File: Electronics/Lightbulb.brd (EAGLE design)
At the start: 65 x 47 mm, 22 parts, among them IC2 7805L

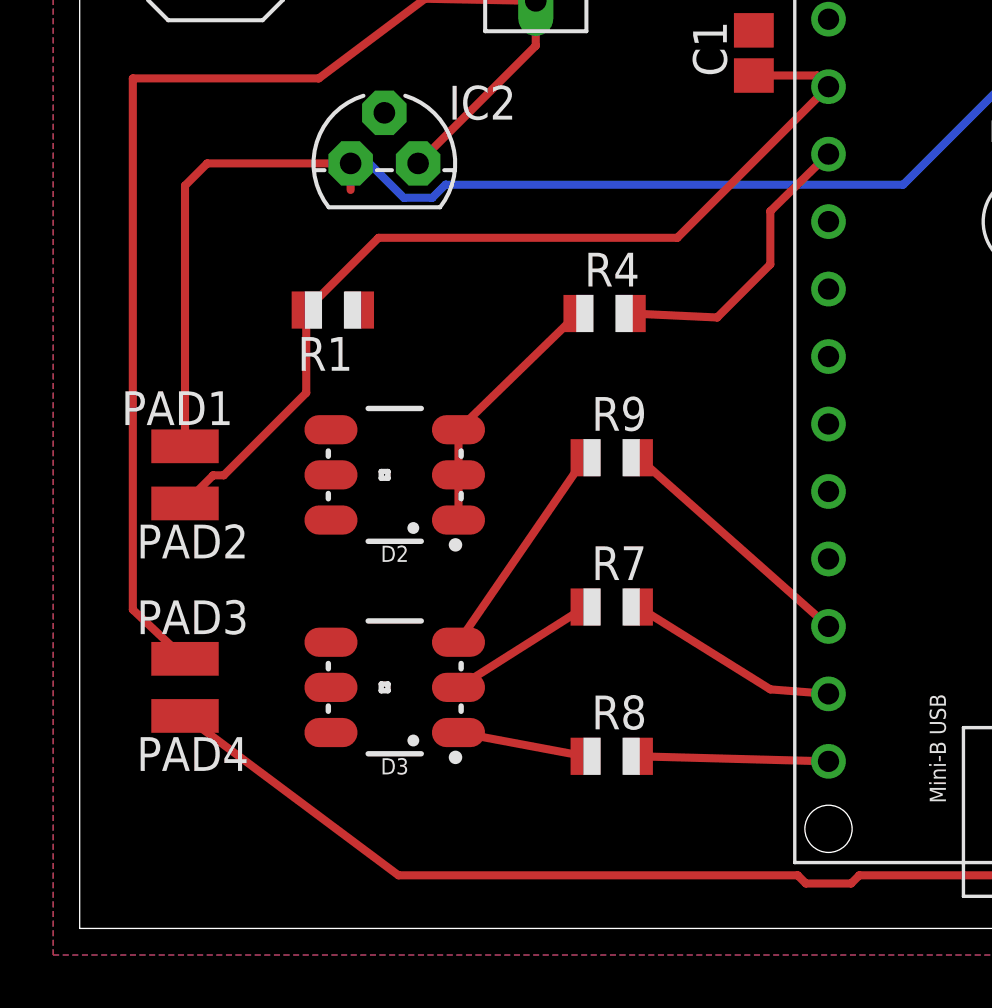
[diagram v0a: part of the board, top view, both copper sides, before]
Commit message: Moving switches and LEDs to bottom side of board
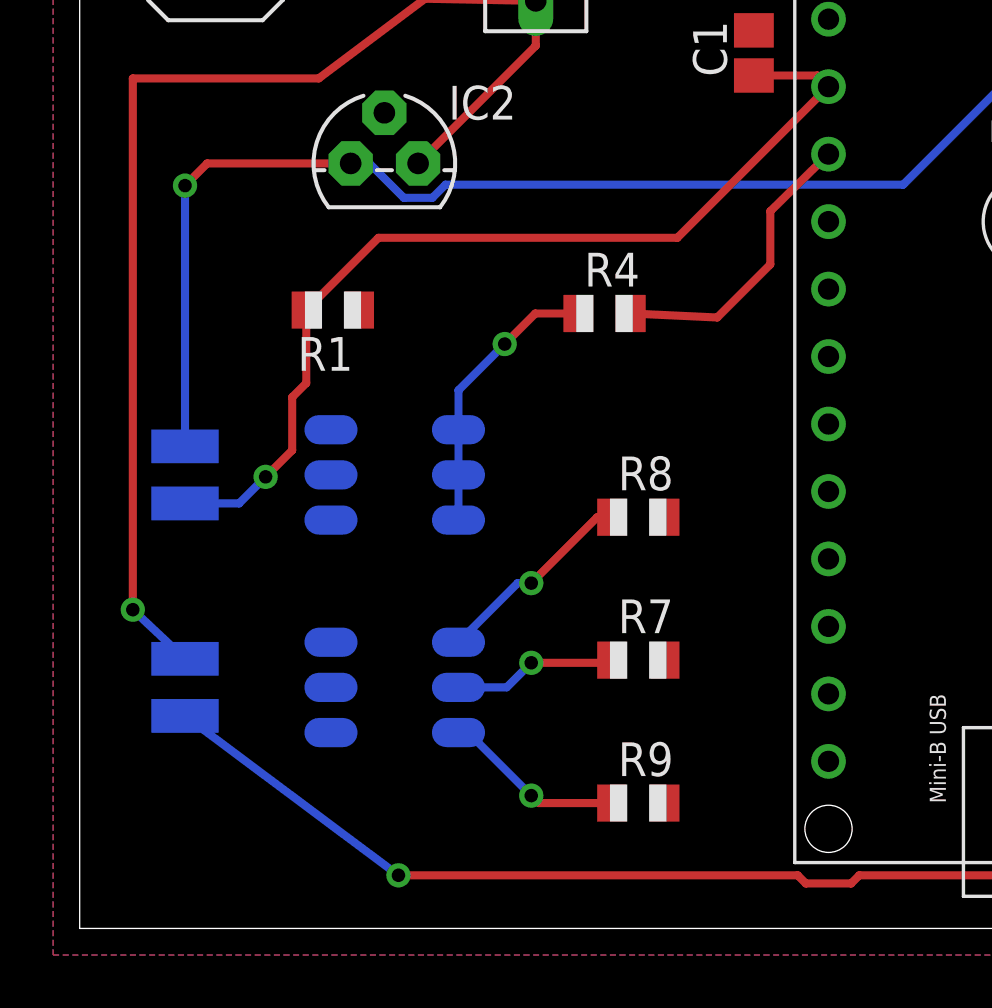
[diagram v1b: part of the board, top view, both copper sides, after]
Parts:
- moved R9 13.0 mm to (21.0, 4.72)
- moved R8 9.06 mm to (21.0, 15.5)
- moved R7 2.24 mm to (21.0, 10.1)
- flipped D2 to the bottom, turned to 0 degrees
- flipped D3 to the bottom, turned to 0 degrees
- flipped PAD1 to the bottom
- flipped PAD2 to the bottom
- flipped PAD3 to the bottom
- flipped PAD4 to the bottom
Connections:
- net N$12: now also ARDUINO_NANO1.28; no longer ARDUINO_NANO1.30
- net N$2: now also ARDUINO_NANO1.30; no longer ARDUINO_NANO1.28
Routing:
- net N$2: track 9.57 -> 0.00 mm
- net N$8: track 8.05 -> 0.00 mm
- net N$12: track 7.16 -> 0.00 mm
- net N$10: track 4.85 -> 7.72 mm, vias 0 -> 1
- net N$11: track 8.43 -> 6.87 mm, vias 0 -> 1
- net N$4: track 68.0 -> 67.0 mm, vias 0 -> 1
- net N$3: track 35.5 -> 36.5 mm, vias 0 -> 1
- net N$18: track 9.68 -> 10.6 mm, vias 0 -> 1
- net N$9: track 5.65 -> 6.19 mm, vias 0 -> 1
- net VCC: vias 0 -> 1
- net N$6: vias 2 -> 3

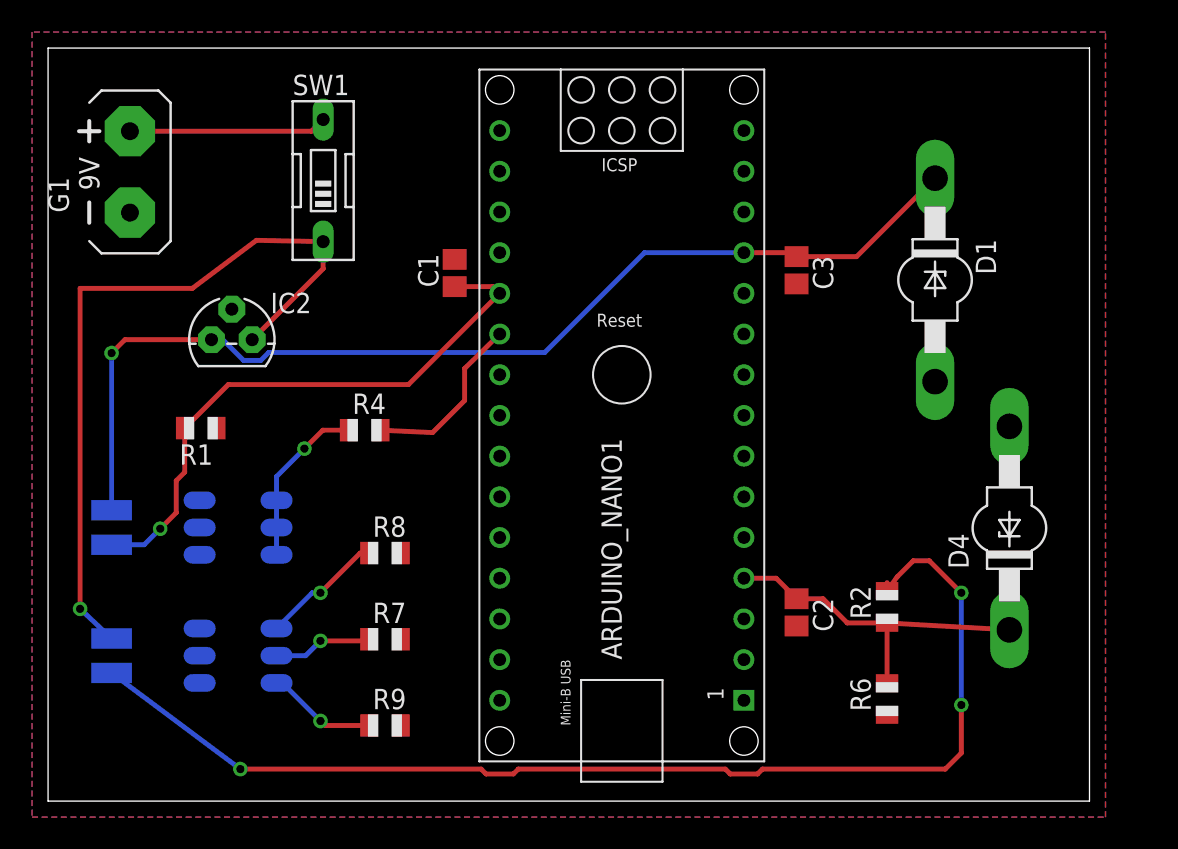
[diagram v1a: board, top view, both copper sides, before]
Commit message: Updated board layout to put master switch on back and added connections for RGB LED
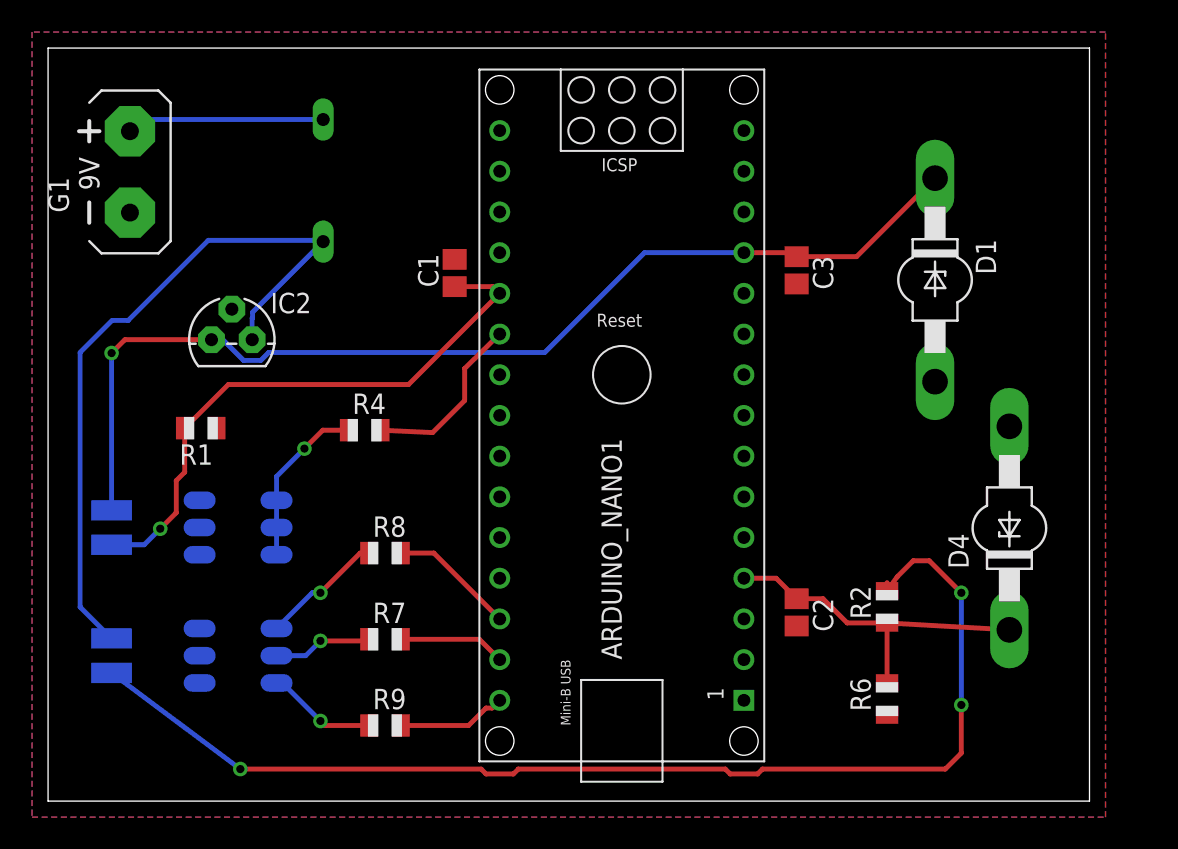
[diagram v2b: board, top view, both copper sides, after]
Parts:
- flipped SW1 to the bottom
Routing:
- net N$12: track 0.00 -> 7.86 mm
- net N$2: track 0.00 -> 6.81 mm
- net N$8: track 0.00 -> 6.69 mm
- net VCC: track 46.8 -> 44.7 mm, vias 1 -> 0
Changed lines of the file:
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@@
 <attribute name="VALUE" x="20.268" y="2.434" size="1.27" layer="27"/>
 </element>
-<element name="SW1" library="special" library_urn="urn:adsk.eagle:library:367" package="EDG-01" package3d_urn="urn:adsk.eagle:package:26661/1" value="" x="17.17" y="38.73">
-<attribute name="NAME" x="15.265" y="44.064" size="1.27" layer="25" ratio="10"/>
-<attribute name="VALUE" x="15.265" y="32.126" size="1.27" layer="27" ratio="10"/>
+<element name="SW1" library="special" library_urn="urn:adsk.eagle:library:367" package="EDG-01" package3d_urn="urn:adsk.eagle:package:26661/1" value="" x="17.17" y="38.73" rot="MR0">
+<attribute name="NAME" x="19.075" y="44.064" size="1.27" layer="26" ratio="10" rot="MR0"/>
+<attribute name="VALUE" x="19.075" y="32.126" size="1.27" layer="28" ratio="10" rot="MR0"/>
 </element>
 </elements>
@@
 <contactref element="IC2" pad="3"/>
 <contactref element="SW1" pad="1"/>
-<wire x1="17.17" y1="33.23" x2="12.74" y2="28.8" width="0.3048" layer="1"/>
-<wire x1="17.17" y1="34.92" x2="13" y2="35" width="0.3048" layer="1"/>
-<wire x1="13" y1="35" x2="9" y2="32" width="0.3048" layer="1"/>
-<wire x1="9" y1="32" x2="2" y2="32" width="0.3048" layer="1"/>
-<wire x1="2" y1="32" x2="2" y2="12" width="0.3048" layer="1"/>
-<wire x1="2" y1="12" x2="3.965" y2="10.15" width="0.3048" layer="16"/>
-<wire x1="17.17" y1="34.92" x2="17.17" y2="33.23" width="0.3048" layer="1"/>
-<via x="2" y="12" extent="1-16" drill="0.508"/>
+<wire x1="17.17" y1="34.92" x2="12.7654" y2="30.5154" width="0.3048" layer="16"/>
+<wire x1="12.7654" y1="30.5154" x2="12.7654" y2="30.168425" width="0.3048" layer="16"/>
+<wire x1="12.7654" y1="30.168425" x2="12.74" y2="30.143025" width="0.3048" layer="16"/>
+<wire x1="12.74" y1="30.143025" x2="12.74" y2="28.8" width="0.3048" layer="16"/>
+<wire x1="17.17" y1="34.92" x2="17.09" y2="35" width="0.3048" layer="16"/>
+<wire x1="5" y1="30" x2="4" y2="30" width="0.3048" layer="16"/>
+<wire x1="4" y1="30" x2="2" y2="28" width="0.3048" layer="16"/>
+<wire x1="2" y1="12.115" x2="3.965" y2="10.15" width="0.3048" layer="16"/>
+<wire x1="17.09" y1="35" x2="10" y2="35" width="0.3048" layer="16"/>
+<wire x1="10" y1="35" x2="5" y2="30" width="0.3048" layer="16"/>
+<wire x1="2" y1="28" x2="2" y2="12.115" width="0.3048" layer="16"/>
 </signal>
 <signal name="N$8">
 <contactref element="R7" pad="2"/>
 <contactref element="ARDUINO_NANO1" pad="29"/>
-<wire x1="22.03" y1="10.1" x2="28.19" y2="8.83" width="0" layer="19" extent="1-1"/>
+<wire x1="22.03" y1="10.1" x2="26.92" y2="10.1" width="0.3048" layer="1"/>
+<wire x1="26.92" y1="10.1" x2="28.19" y2="8.83" width="0.3048" layer="1"/>
 </signal>
 <signal name="N$1">
 <contactref element="G1" pad="+"/>
 <contactref element="SW1" pad="2"/>
-<wire x1="5.11" y1="41.81" x2="16.44" y2="41.81" width="0.3048" layer="1"/>
-<wire x1="16.44" y1="41.81" x2="17.17" y2="42.54" width="0.3048" layer="1"/>
+<wire x1="17.17" y1="42.54" x2="5.84" y2="42.54" width="0.3048" layer="16"/>
+<wire x1="5.84" y1="42.54" x2="5.11" y2="41.81" width="0.3048" layer="16"/>
 </signal>
 <signal name="N$2">
 <contactref element="ARDUINO_NANO1" pad="30"/>
 <contactref element="R9" pad="2"/>
-<wire x1="22.03" y1="4.72" x2="28.19" y2="6.29" width="0" layer="19" extent="1-1"/>
+<wire x1="22.03" y1="4.72" x2="26.25039375" y2="4.72" width="0.3048" layer="1"/>
+<wire x1="26.25039375" y1="4.72" x2="27.33779375" y2="5.8074" width="0.3048" layer="1"/>
+<wire x1="27.33779375" y1="5.8074" x2="27.7074" y2="5.8074" width="0.3048" layer="1"/>
+<wire x1="27.7074" y1="5.8074" x2="28.19" y2="6.29" width="0.3048" layer="1"/>
 </signal>
 <signal name="N$12">
 <contactref element="R8" pad="2"/>
 <contactref element="ARDUINO_NANO1" pad="28"/>
-<wire x1="22.03" y1="15.48" x2="28.19" y2="11.37" width="0" layer="19" extent="1-1"/>
+<wire x1="22.03" y1="15.48" x2="24.08" y2="15.48" width="0.3048" layer="1"/>
+<wire x1="24.08" y1="15.48" x2="28.19" y2="11.37" width="0.3048" layer="1"/>
 </signal>
 </signals>

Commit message: Correcting pad placement and connections on PCB
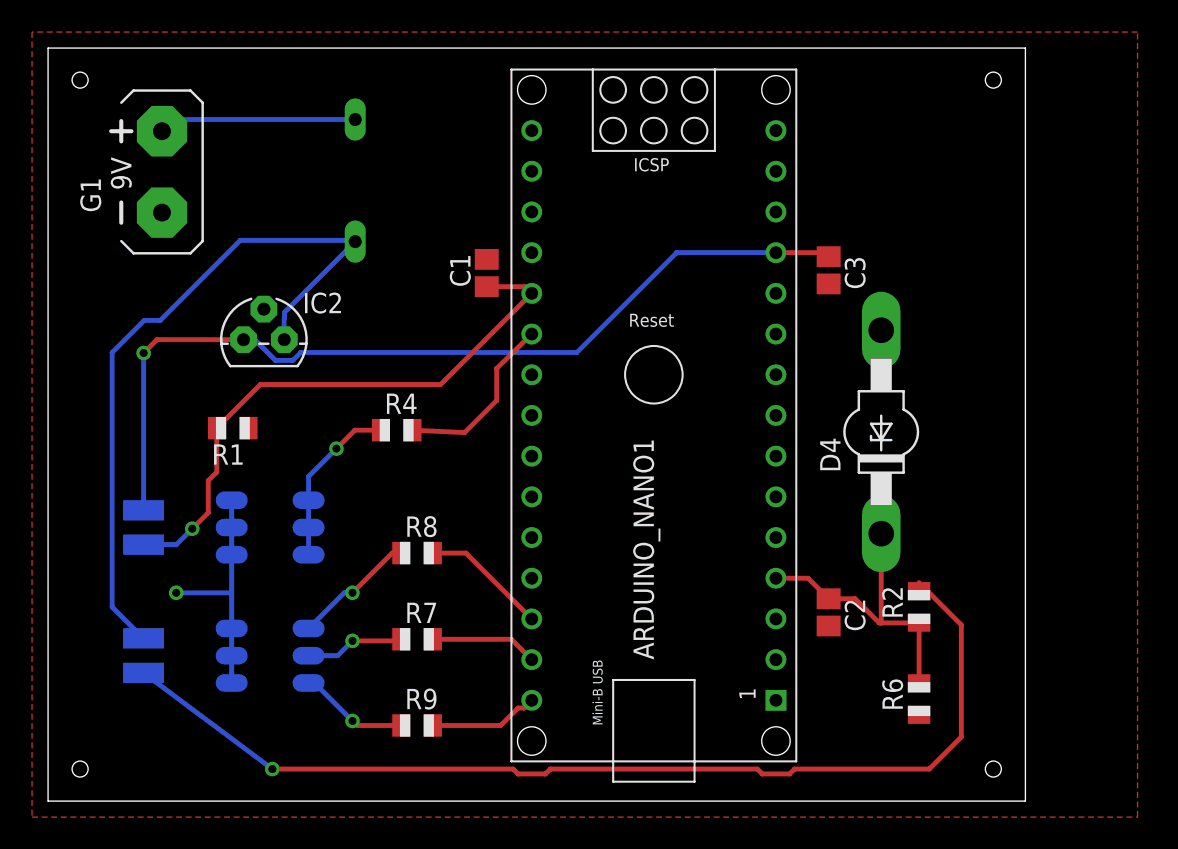
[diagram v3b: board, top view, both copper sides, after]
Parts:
- removed D1: 5.1V Zener, diode:SOD64Z12
- moved D4 10.0 mm to (52.0, 23.0)
- moved ARDUINO_NANO1 2.00 mm to (37.8, 26.6)
- moved C1 2.00 mm to (27.4, 33.0)
- moved C2 2.00 mm to (48.7, 11.8)
- moved C3 2.00 mm to (48.7, 33.1)
- moved D2 2.00 mm to (13.9, 17.1)
- moved D3 2.00 mm to (13.9, 9.07)
- moved G1 2.00 mm to (7.11, 39.3)
- moved IC2 2.00 mm to (13.5, 28.8)
- moved PAD1 2.00 mm to (5.96, 18.1)
- moved PAD2 2.00 mm to (5.96, 16.0)
- moved PAD3 2.00 mm to (5.96, 10.2)
- moved PAD4 2.00 mm to (5.96, 8.00)
- moved R1 2.00 mm to (11.5, 23.3)
- moved R2 2.00 mm to (54.4, 12.1)
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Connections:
- net GND: no longer D1.A
- net N$4: no longer D1.C
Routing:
- net GND: track 0.00 -> 14.9 mm, vias 0 -> 1
- net N$4: track 67.0 -> 56.3 mm
- net N$6: track 72.8 -> 65.4 mm, vias 3 -> 1
- net N$5: track 21.5 -> 19.4 mm
- removed copper zone on layer 16, net GND
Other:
- board size 65 x 47 mm -> 61 x 47 mm

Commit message: Moving small components further from MCU on board, tweaking ADC part of code for battery tester
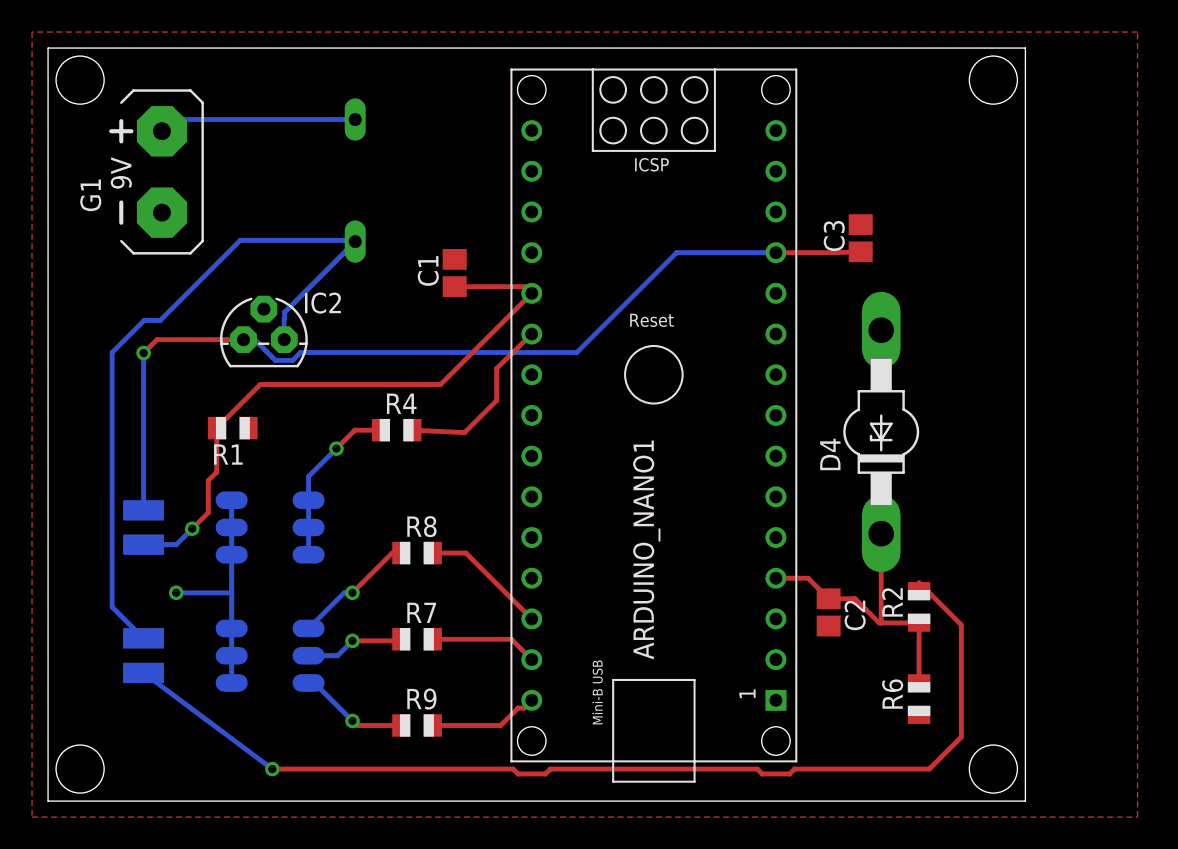
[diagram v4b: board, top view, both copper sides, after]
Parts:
- moved C3 2.83 mm to (50.7, 35.1), turned to 90 degrees
- moved C1 2.00 mm to (25.4, 33.0)
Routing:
- net N$3: track 36.5 -> 38.5 mm
- net N$4: track 56.3 -> 58.2 mm
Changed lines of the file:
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@@
 <wire x1="61" y1="47" x2="0" y2="47" width="0" layer="20"/>
 <wire x1="0" y1="47" x2="0" y2="0" width="0" layer="20"/>
-<hole x="2" y="45" drill="1"/>
-<hole x="2" y="2" drill="1"/>
-<hole x="59" y="2" drill="1"/>
-<hole x="59" y="45" drill="1"/>
+<hole x="2" y="45" drill="3"/>
+<hole x="2" y="2" drill="3"/>
+<hole x="59" y="2" drill="3"/>
+<hole x="59" y="45" drill="3"/>
 </plain>
 <attributes>
@@
 <attribute name="VALUE" x="40.35" y="8.83" size="1.27" layer="21" font="vector" rot="R90"/>
 </element>
-<element name="C1" library="adafruit" package="C0805" value="0.1¨µF" x="27.38" y="32.96" rot="R90">
-<attribute name="NAME" x="26.364" y="32.071" size="1.27" layer="25" rot="R90"/>
-<attribute name="VALUE" x="29.666" y="32.071" size="1.27" layer="27" rot="R90"/>
+<element name="C1" library="adafruit" package="C0805" value="0.1¨µF" x="25.38" y="32.96" rot="R90">
+<attribute name="NAME" x="24.364" y="32.071" size="1.27" layer="25" rot="R90"/>
+<attribute name="VALUE" x="27.666" y="32.071" size="1.27" layer="27" rot="R90"/>
 </element>
 <element name="C2" library="adafruit" package="C0805" value="0.1µF" x="48.72" y="11.78" rot="R270">
@@
 <attribute name="VALUE" x="46.434" y="12.669" size="1.27" layer="27" rot="R270"/>
 </element>
-<element name="C3" library="adafruit" package="C0805" value="0.1µF" x="48.72" y="33.13" rot="R270">
-<attribute name="NAME" x="49.736" y="34.019" size="1.27" layer="25" rot="R270"/>
-<attribute name="VALUE" x="46.434" y="34.019" size="1.27" layer="27" rot="R270"/>
+<element name="C3" library="adafruit" package="C0805" value="0.1µF" x="50.72" y="35.13" rot="R90">
+<attribute name="NAME" x="49.704" y="34.241" size="1.27" layer="25" rot="R90"/>
+<attribute name="VALUE" x="53.006" y="34.241" size="1.27" layer="27" rot="R90"/>
 </element>
 <element name="D2" library="SparkFun-LED" library_urn="urn:adsk.eagle:library:529" package="LED-TRICOLOR-5050" package3d_urn="urn:adsk.eagle:package:39374/1" value="WHITE LED" x="13.86" y="17.075" rot="MR0">
@@
 <wire x1="30.19" y1="31.69" x2="24.5" y2="26" width="0.3048" layer="1"/>
 <wire x1="24.5" y1="26" x2="13.25" y2="26" width="0.3048" layer="1"/>
-<wire x1="29.77" y1="32.11" x2="27.38" y2="32.11" width="0.3048" layer="1"/>
+<wire x1="29.77" y1="32.11" x2="25.38" y2="32.11" width="0.3048" layer="1"/>
 <wire x1="30.19" y1="31.69" x2="29.77" y2="32.11" width="0.3048" layer="1"/>
 <wire x1="8" y1="16" x2="5.965" y2="16" width="0.3048" layer="16"/>
@@
 <wire x1="5.965" y1="27.965" x2="5.965" y2="18.15" width="0.3048" layer="16"/>
 <wire x1="6.8" y1="28.8" x2="5.965" y2="27.965" width="0.3048" layer="1"/>
-<wire x1="48.72" y1="33.98" x2="48.47" y2="34.23" width="0.3048" layer="1"/>
-<wire x1="48.47" y1="34.23" x2="45.43" y2="34.23" width="0.3048" layer="1"/>
+<wire x1="50.72" y1="34.28" x2="48.97" y2="34.23" width="0.3048" layer="1"/>
+<wire x1="48.97" y1="34.23" x2="45.43" y2="34.23" width="0.3048" layer="1"/>
 <wire x1="15.276575" y1="27.5046" x2="14.203425" y2="27.5046" width="0.3048" layer="16"/>
 <wire x1="12.908025" y1="28.8" x2="12.2" y2="28.8" width="0.3048" layer="16"/>

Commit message: Updating board with custom-made footprints for push buttons
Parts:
- removed PAD1: BUSHBUTTON 1, wirepad:SMD1,27-2,54
- removed PAD2: PUSHBUTTON 1, wirepad:SMD1,27-2,54
- removed PAD3: BUSHBUTTON 2, wirepad:SMD1,27-2,54
- removed PAD4: PUSHBUTTON 2, wirepad:SMD1,27-2,54
- added U$1, U$2: SKRPABE010, Custom Library:SKRPABE010
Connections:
- net N$3: now also U$1.3, U$1.4; no longer PAD2.1
- net N$4: now also U$1.1, U$1.2; no longer PAD1.1
- net N$6: now also U$2.3, U$2.4; no longer PAD4.1
- net VCC: now also U$2.1, U$2.2; no longer PAD3.1
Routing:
- net N$6: track 65.4 -> 73.6 mm
- net VCC: track 44.7 -> 49.3 mm
- net N$3: track 38.5 -> 41.6 mm
- net N$4: track 58.2 -> 60.2 mm
